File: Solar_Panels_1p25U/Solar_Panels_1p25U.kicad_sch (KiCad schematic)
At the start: 62 parts, among them J1 Conn_01x08_MountingPin, J2 Conn_01x08_MountingPin, J3 Conn_01x08_MountingPin, J4 Conn_01x02, J5 Conn_01x08_MountingPin

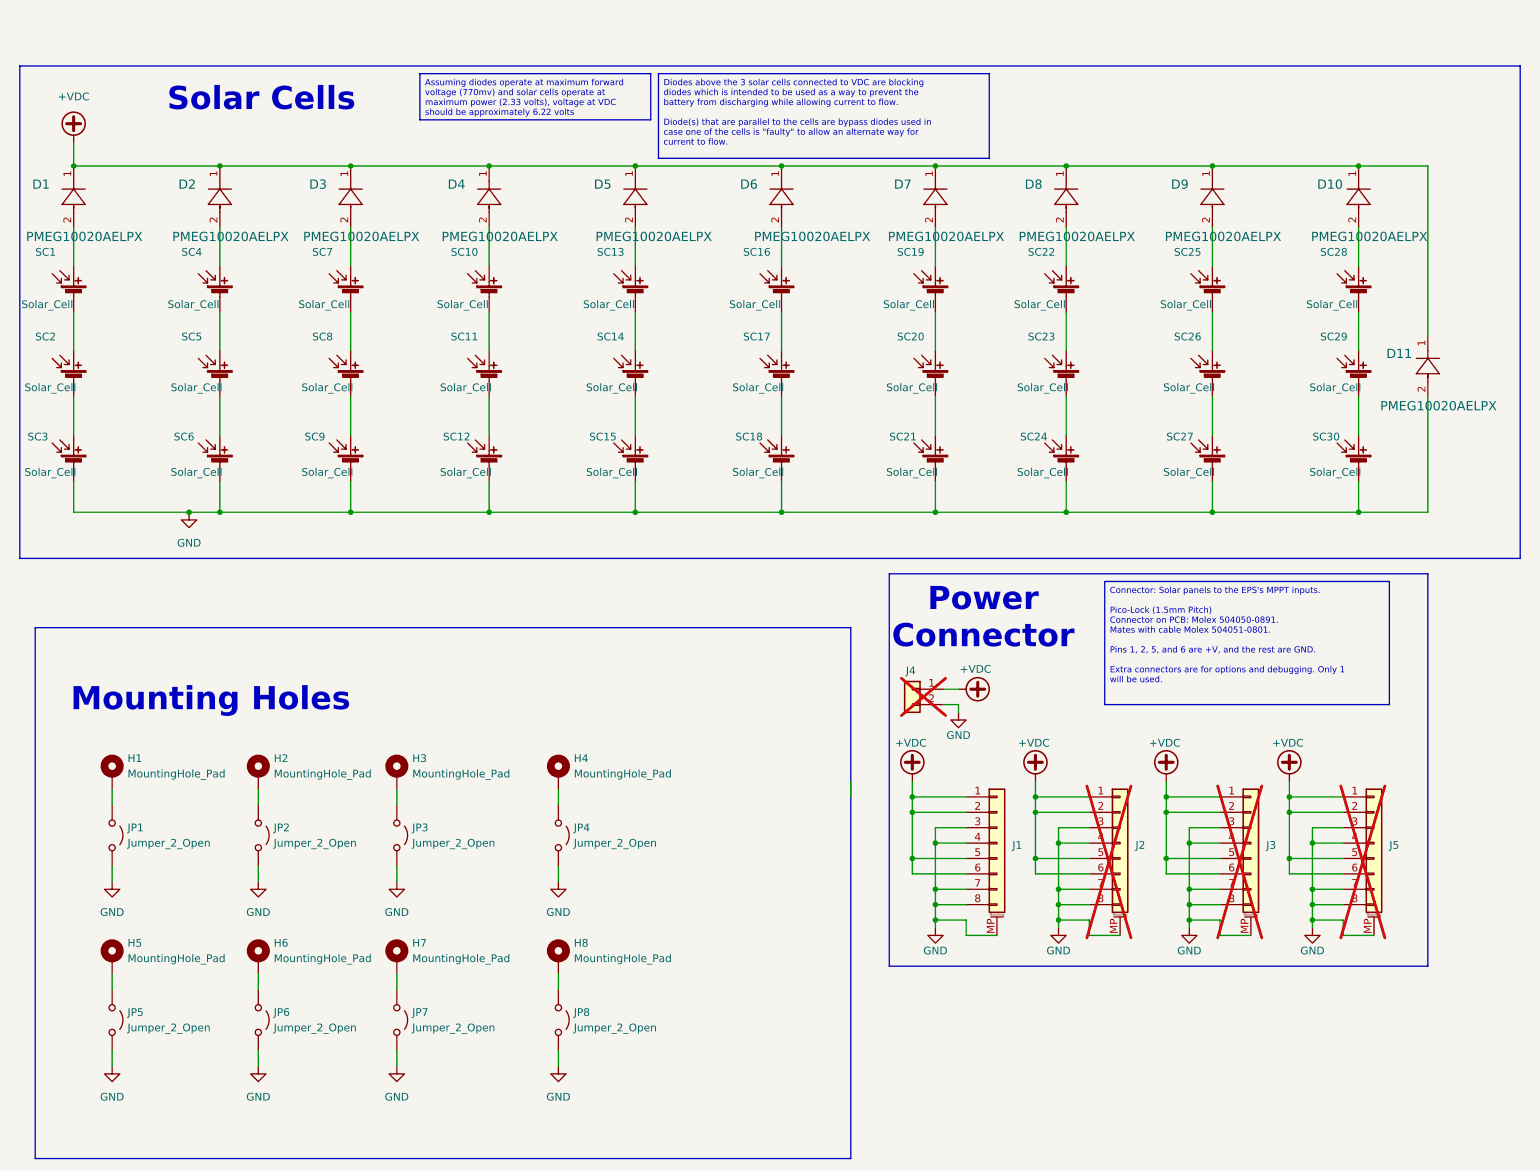
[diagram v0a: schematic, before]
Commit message: Design new Rev 2 solar panel with new cells
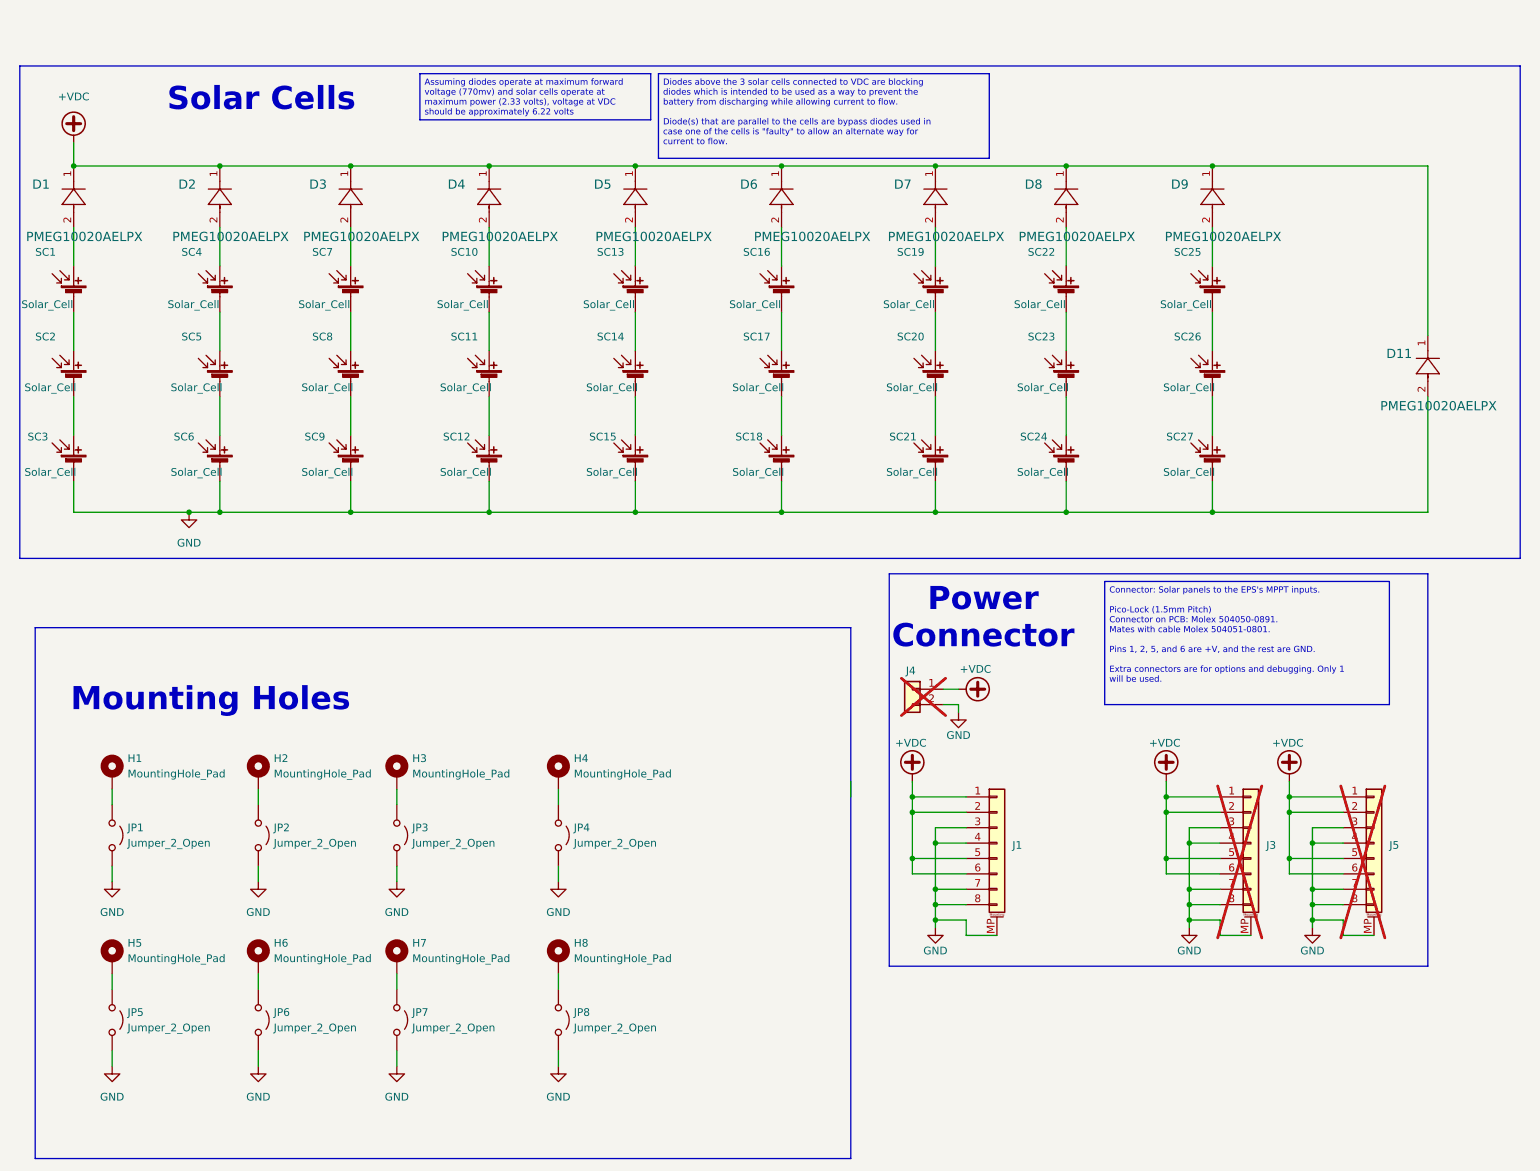
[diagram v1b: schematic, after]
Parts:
- removed D10: PMEG10020AELPX, Solar Panel Library:PMEG10020AELPX, symbol Lib:S3B_R1_00001
- removed J2: Conn_01x08_MountingPin, Connector_Molex:Molex_PicoBlade_53261-0871_1x08-1MP_P1.25mm_Horizontal, symbol Connector_Generic_MountingPin:Conn_01x08_MountingPin
- removed SC28, SC29, SC30: Solar_Cell, Solar Panel Library:TrisolX Solar Wings, symbol Device:Solar_Cell
- SC1, SC10, SC11, SC12, SC13, SC14, SC15, SC16, SC17, SC18, SC19, SC2, SC20, SC21, SC22, SC23, SC24, SC25, SC26, SC27, SC3, SC4, SC5, SC6, SC7, SC8, SC9: footprint Solar Panel Library:TrisolX Solar Wings -> Solar Panel Library:KXOB25-05X3F

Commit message: Finish routing
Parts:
- removed D1: PMEG10020AELPX, Solar Panel Library:PMEG10020AELPX, symbol Lib:S3B_R1_00001
- SC1, SC10, SC11, SC12, SC13, SC14, SC15, SC16, SC17, SC18, SC19, SC2, SC20, SC21, SC22, SC23, SC24, SC25, SC26, SC27, SC3, SC4, SC5, SC6, SC7, SC8, SC9: value Solar_Cell -> KXOB25-05X3F
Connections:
- net +VDC: now also SC1.1 (+)
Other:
- title: TriSolX 1.25U Solar Panel -> 1.25U Solar Panel
- moved on the sheet: H1, H2, H3, H4, H5, H6, H7, H8, JP1, JP2, JP3, JP4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

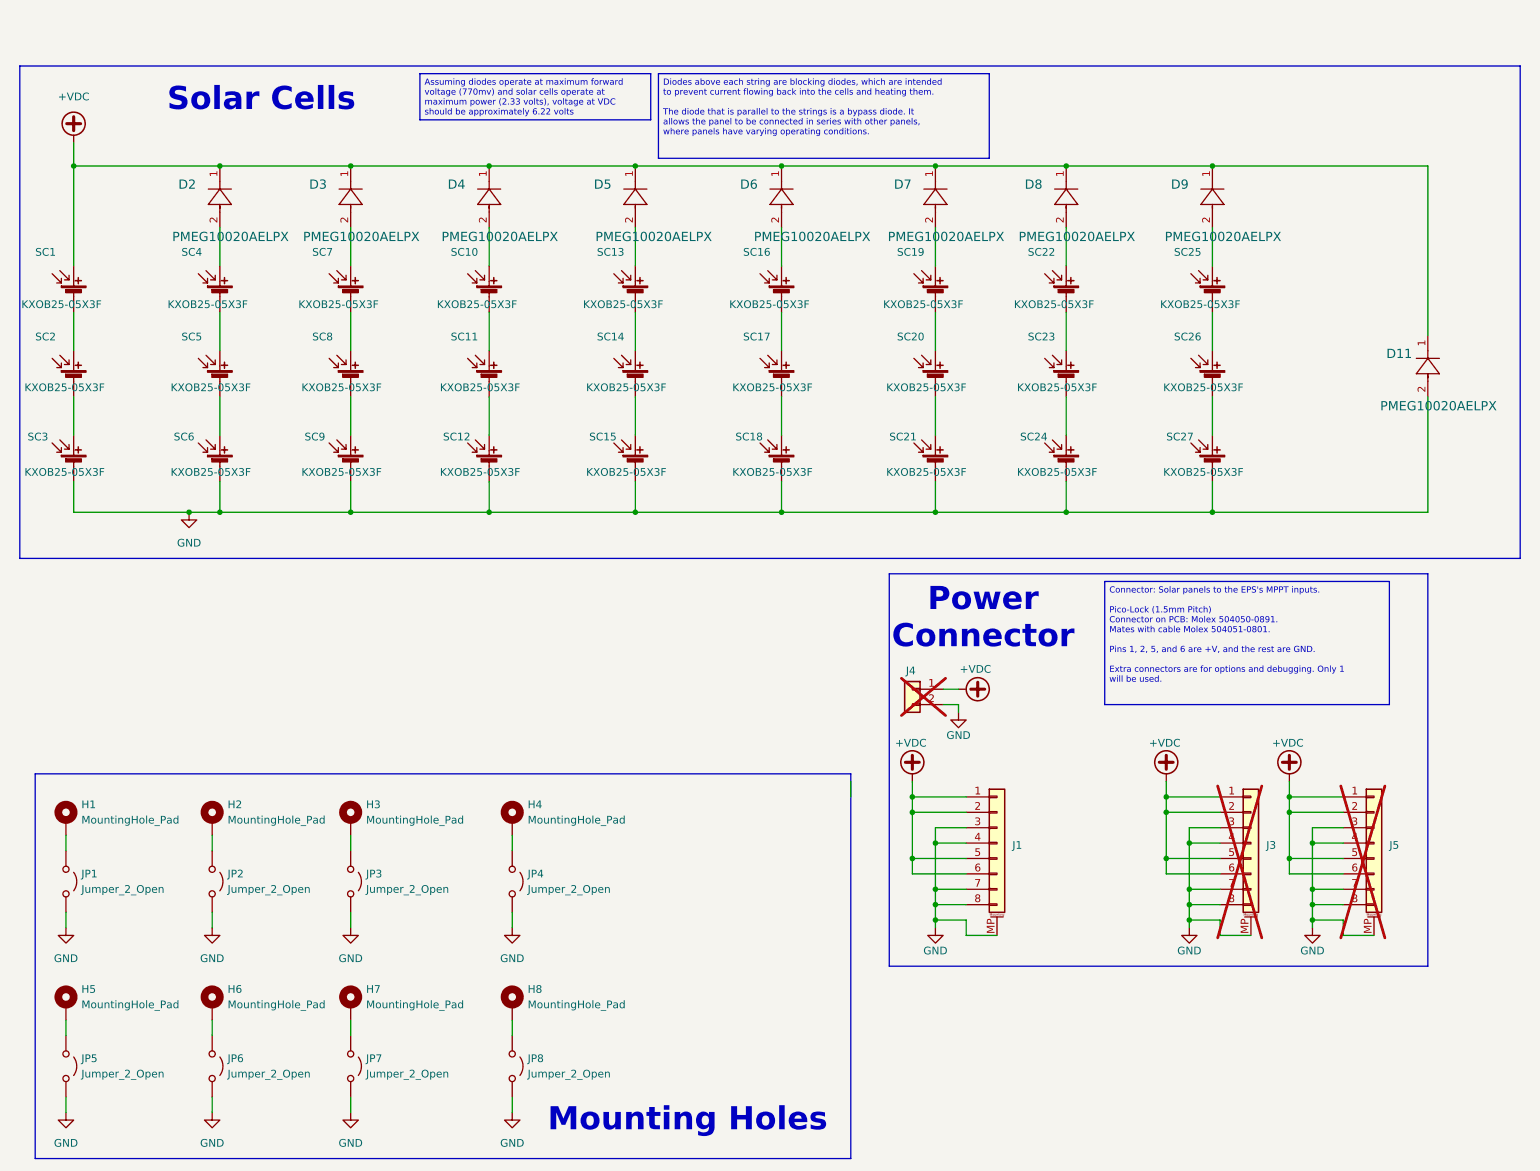
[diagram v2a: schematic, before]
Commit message: Update footprints with extra protuding pads for testing
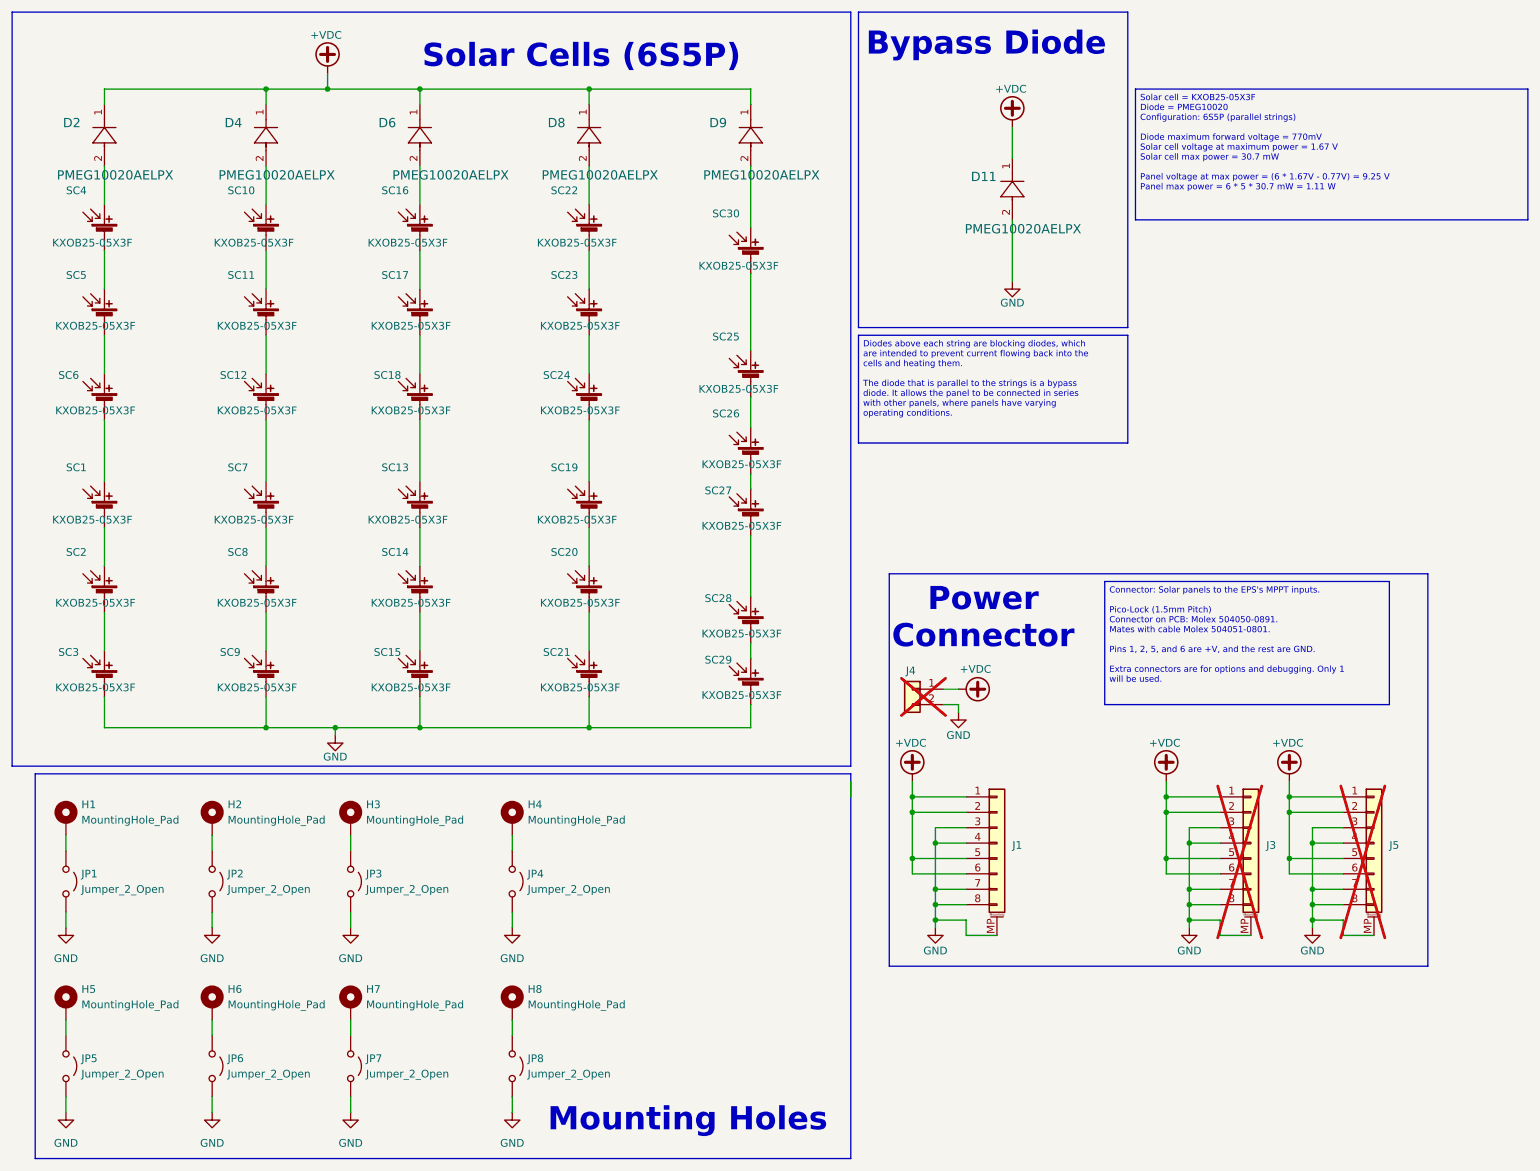
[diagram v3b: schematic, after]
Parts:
- removed D3, D5, D7: PMEG10020AELPX, Solar Panel Library:PMEG10020AELPX, symbol Lib:S3B_R1_00001
- added SC28, SC29, SC30: KXOB25-05X3F, Solar Panel Library:KXOB25-05X3F, symbol Device:Solar_Cell
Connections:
- net +VDC: no longer SC1.1 (+)
- net GND: now also SC29.2 (-); no longer SC12.2 (-), SC18.2 (-), SC24.2 (-), SC27.2 (-), SC6.2 (-)
- net at SC13.1 (+): now also SC18.2 (-)
- net at SC7.1 (+): now also SC12.2 (-)
- net at D9.2: now also SC30.1 (+); no longer SC25.1 (+)
- net at SC19.1 (+): now also SC24.2 (-)
- new net: SC25.1 (+), SC30.2 (-)
- new net: SC27.2 (-), SC28.1 (+)
- new net: SC1.1 (+), SC6.2 (-)
- new net: SC28.2 (-), SC29.1 (+)
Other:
- note added: "Bypass Diode"
- note added: "Solar Cells (6S5P)"
- note removed: "Solar Cells"
- moved on the sheet: D11, D2, D4, D6, D8, D9, SC1, SC10, SC11, SC12, SC13, SC14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

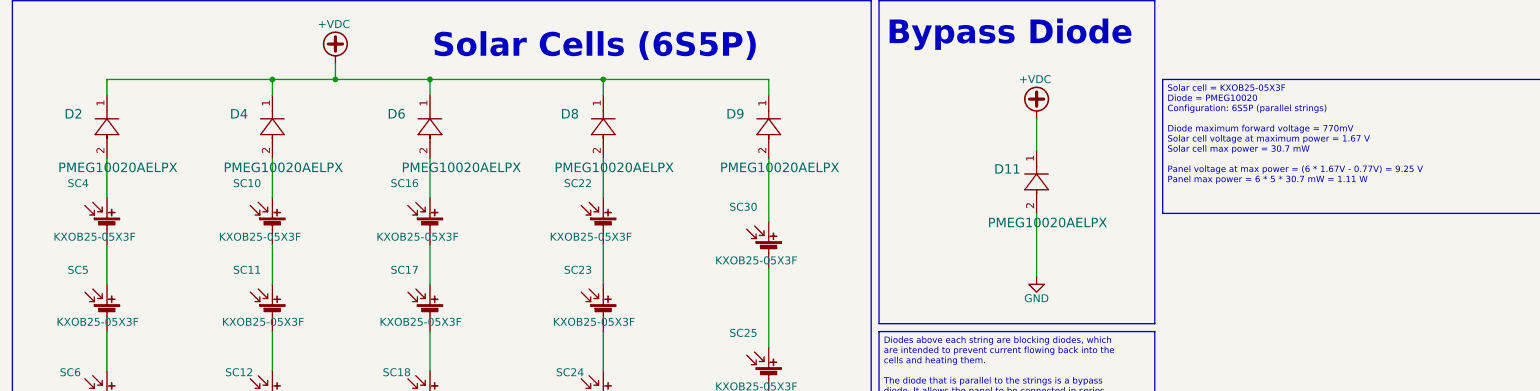
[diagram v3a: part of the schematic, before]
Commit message: Update diode model and description
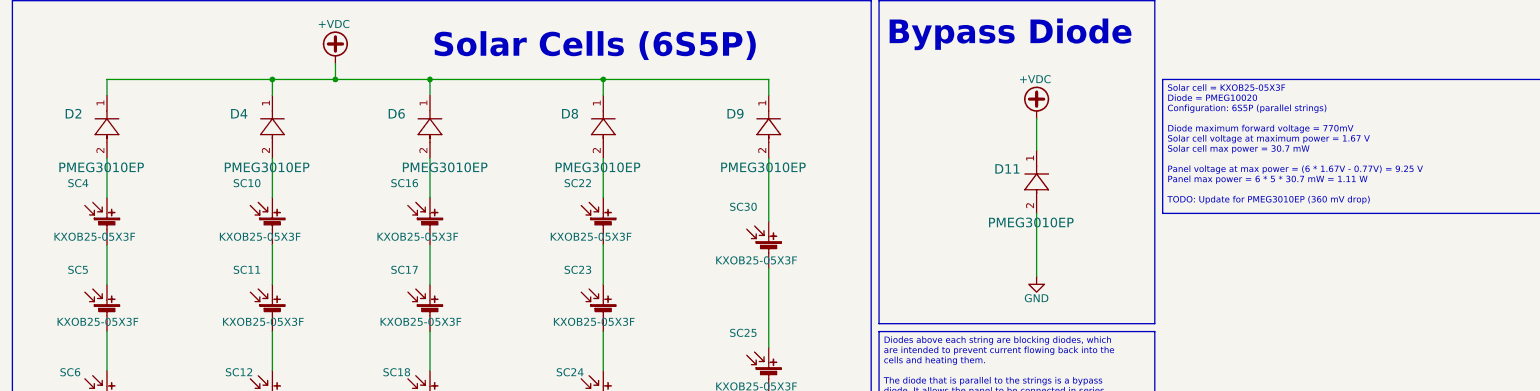
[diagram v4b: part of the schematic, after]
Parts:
- D11, D2, D4, D6, D8, D9: value PMEG10020AELPX -> PMEG3010EP
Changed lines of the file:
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@@
 		)
 	)
-	(text_box "Solar cell = KXOB25-05X3F\nDiode = PMEG10020\nConfiguration: 6S5P (parallel strings)\n\nDiode maximum forward voltage = 770mV\nSolar cell voltage at maximum power = 1.67 V\nSolar cell max power = 30.7 mW\n\nPanel voltage at max power = (6 * 1.67V - 0.77V) = 9.25 V\nPanel max power = 6 * 5 * 30.7 mW = 1.11 W"
+	(text_box "Solar cell = KXOB25-05X3F\nDiode = PMEG10020\nConfiguration: 6S5P (parallel strings)\n\nDiode maximum forward voltage = 770mV\nSolar cell voltage at maximum power = 1.67 V\nSolar cell max power = 30.7 mW\n\nPanel voltage at max power = (6 * 1.67V - 0.77V) = 9.25 V\nPanel max power = 6 * 5 * 30.7 mW = 1.11 W\n\nTODO: Update for PMEG3010EP (360 mV drop)"
 		(exclude_from_sim no)
 		(at 199.39 25.4 0)
@@
 			"SCSTthil9JfdDgAAAAB45RhjL/V5vJUEAAAAAInoy2ZPAAAAAAAtvJUEAAAAAIkQJQEAAABAIkRJ"
 			"AAAAAJAIURIAAAAAJEKUBAAAAACJECUBAAAAQCJESQAAAACQCFESAAAAACRClAQAAAAAiRAlAQAA"
-			"AEAiREkAAAAAkOh/DwIXO4Usz7AAAAAASUVORK5CYII="
+			"AEAiREkAAAAAkOh/DwIXO4Usz7AAAAAASUVORK5CYIL/UCQ2XORiAAAAAAAAAAAAAAAAAAAAAAAA"
+			"AAAAAAAAAAAAAAAAAAAAAP//////////ECY2XORiAAAAAAAAAAAAAAAAAAAAAAAAAAAAAAAAAAAA"
+			"AAAAAAAAAAAAAAAAAAAAAAAAAAAAAAAAAAAAAAAAAAAAAAAAAAAA//////////8QJDZc5GIAAAAA"
+			"AAAAAAAAAAAAAAAAAAAAAAAAAAAAAAAAAAAAAAAA//////////8wJzZc5GIAAAAAAAAAAAAAAAAA"
+			"AAAAAAD//////////xAnNlzkYgAA//////////9wJjZc5GIAAP//////////8CY2XORiAAAAAAAA"
+			"AAAAAAAAAAAAAAAAAAAAAAAAAAAAAAAAAAAAAAAAAAAAAAAAAAAAAAAAAAAAAAAAAAAAAAAAAAAA"
+			"AAAAAAAAAAAAAAAAAAAAAAAAAP//////////UCM2XORiAAAAAAAAAAAAAAAAAAAAAAAAAAAAAAAA"
+			"AAAAAAAAAAAAAAAAAAAAAAAAAAAAAAAAAAAAAAAAAAAAAAAAAAAAAAAA//////////8wJDZc5GIA"
+			"AP//////////sCU2XORiAAAAAAAAAAAAAAAAAAAAAAAA///////////wJTZc5GIAAAAAAAAAAAAA"
+			"UB8/sKN6AAAAAAAAAAAAAIDSi1HkYgAA//////////9QJTZc5GIAAAAAAAAAAAAA1gAAABIAAAD/"
+			"/////////9AkNlzkYgAAAAAAAAAAAADWAAAAo3oAACAIAAAAAAAAEAQAAAAAAAAA8P///////4Bg"
+			"NlzkYgAAAPD////////gYjZc5GIAAADw////////YF82XORiAAAA8P///////wBgNlzkYgAAAPD/"
+			"//////+AYzZc5GIAAADw////////YGA2XORiAAAA8P///////yBfNlzkYgAAAPD/////////////"
+			"5GIAAADw////////IGI2XORiAAAA8P///////6BjNlzkYgAAAPD///////9AXzZc5GIAAADw////"
+			"////oF82XORiAAAA8P///////+BgNlzkYgAAAPD///////8AYzZc5GIAAADw////////wGI2XORi"
+			"AAAA8P///////wBiNlzkYgAAAPD///////+AwjRc5GIAAADw////////wGQ2XORiAAAA8P//////"
+			"/0BkNlzkYgAAAPD///////9AyTRc5GIAAADw////////YGE2XORiAAAA8P///////wIAAAD/////"
+			"APD////////I7gxG5GIAAADw////////QNokR+RiAAAA8P///////6BiNlzkYgAAAPD////////A"
+			"YDZc5GIAAADw////////IGA2XORiAAAA8P///////w=="
 		)
 	)
@@
 			)
 		)
-		(property "Value" "PMEG10020AELPX"
+		(property "Value" "PMEG3010EP"
 			(at 101.346 39.624 90)
 			(effects
@@
 			)
 		)
-		(property "Value" "PMEG10020AELPX"
+		(property "Value" "PMEG3010EP"
 			(at 76.708 39.624 90)
 			(effects
@@
 			)
 		)
-		(property "Value" "PMEG10020AELPX"
+		(property "Value" "PMEG3010EP"
 			(at 171.196 48.514 90)
 			(effects
@@
 			)
 		)
-		(property "Value" "PMEG10020AELPX"
+		(property "Value" "PMEG3010EP"
 			(at 128.016 39.624 90)
 			(effects
@@
 			)
 		)
-		(property "Value" "PMEG10020AELPX"
+		(property "Value" "PMEG3010EP"
 			(at 21.336 39.624 90)
 			(effects
@@
 			)
 		)
-		(property "Value" "PMEG10020AELPX"
+		(property "Value" "PMEG3010EP"
 			(at 48.006 39.624 90)
 			(effects
